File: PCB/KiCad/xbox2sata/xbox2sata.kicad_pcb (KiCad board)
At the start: 4 copper layers, 33 x 58.9 mm, 47 parts, among them J1 929975-01-20-RK, J2 61203921621, J3 SATA-A-PL-SMT-K, U1 1V2 voltage regulator, U5 88SA8052, Y1 25MHz

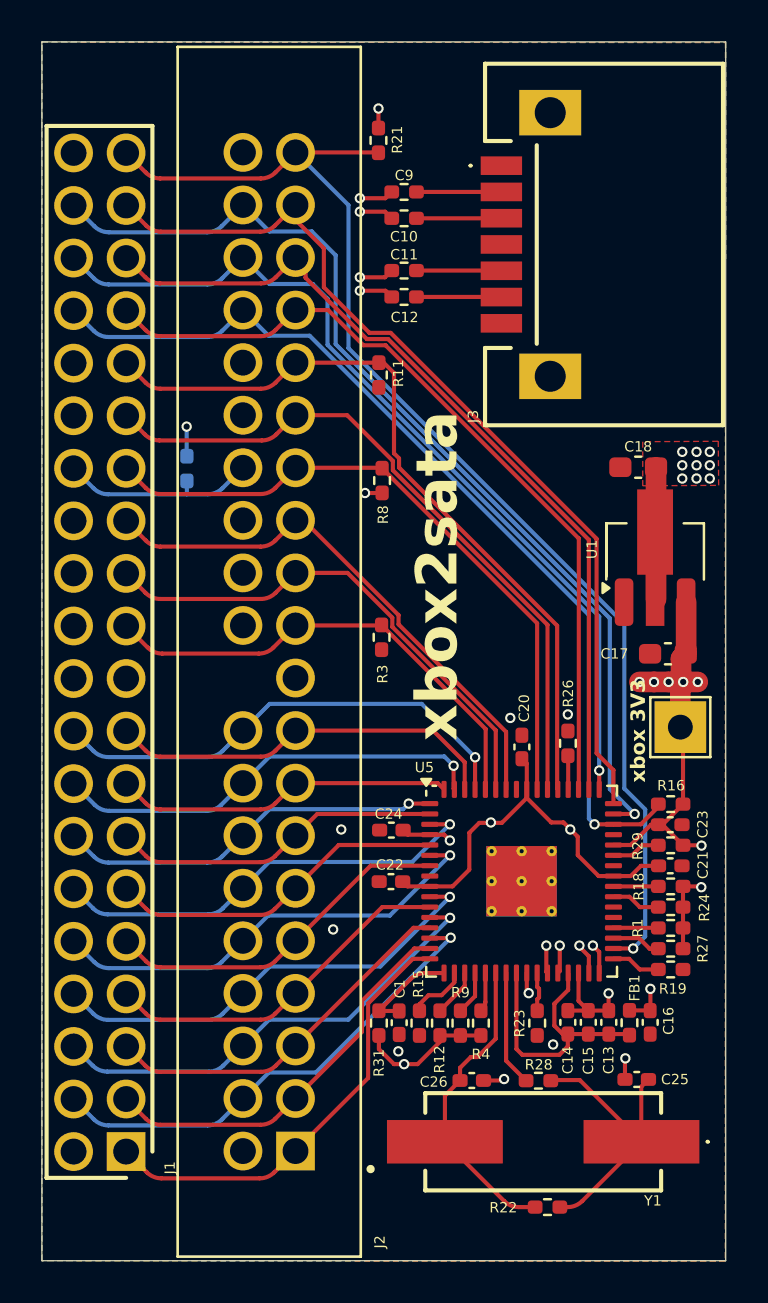
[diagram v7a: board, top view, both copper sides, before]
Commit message: Reset-Negative was not enabled
10K resistor (R14) pull-up to 3V3 added to CSEL IDE pin 28
4.7K resistor (R19) pull-down to ground on T0 U5 pin 33 to device as IDE master
Positive power supply icons changed from Global labels to Power symbols

Via sizes changed to 0.3 and 0.5 mm for jlcpcb requirements
Bill of materials updated
Mouser shared basket created;
https://www.mouser.co.uk/api/CrossDomain/GetContext?syncDomains=www&returnUrl=https%3a%2f%2fwww.mouser.com%2fProjectManager%2fProjectDetail.aspx%3fAccessID%3da2276a8976&async=False&setPrefSub=False&clearPrefSub=False
Datasheets added
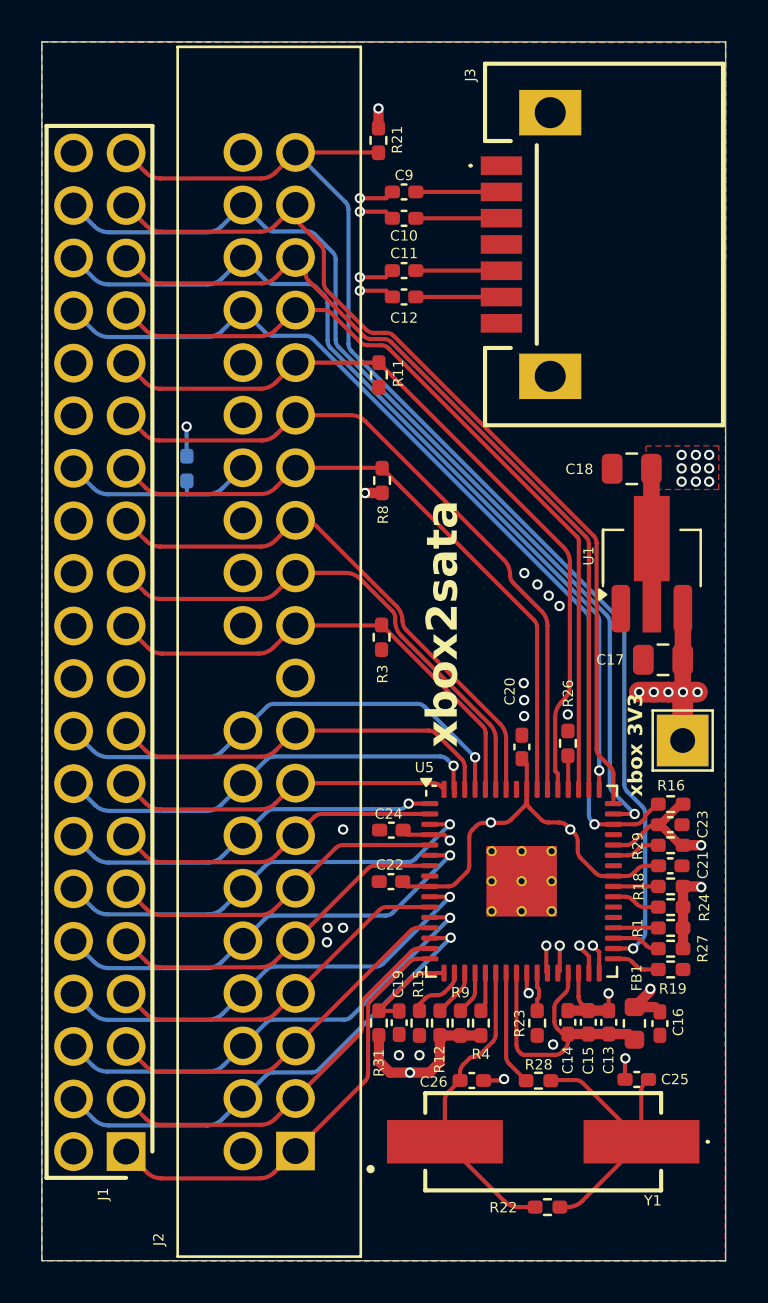
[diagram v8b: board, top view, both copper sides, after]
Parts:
- C10, C11, C12, C9: footprint Resistor_SMD:R_0402_1005Metric_Pad0.72x0.64mm_HandSolder -> Capacitor_SMD:C_0402_1005Metric_Pad0.74x0.62mm_HandSolder
- C17, C18: footprint Capacitor_SMD:C_0603_1608Metric_Pad1.08x0.95mm_HandSolder -> Capacitor_SMD:C_0805_2012Metric
- C25, C26: value 18pF -> 16pF
- FB1: value 60R -> 120R; footprint Resistor_SMD:R_0402_1005Metric_Pad0.72x0.64mm_HandSolder -> Inductor_SMD:L_0603_1608Metric
- moved TP2 0.66 mm to (135.1, 90.6)
- moved C16 0.47 mm to (133.9, 104.3)
- moved C17 0.37 mm to (134.1, 86.7)
- moved U1 0.35 mm to (133.6, 81.8)
- moved C18 0.32 mm to (132.6, 77.5)
- moved FB1 0.24 mm to (132.7, 104.3)
- renumbered C1 to C19
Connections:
- J1 pad 20: GND -> unconnected-(J1-Pad20)
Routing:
- net TX_P: track 53.3 -> 51.5 mm
- net +3V3: track 37.1 -> 35.7 mm
- net GND: vias 6 -> 15
- added copper zone on In2.Cu, net GND
